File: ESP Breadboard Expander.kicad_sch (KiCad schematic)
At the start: 20 parts, among them J1 Conn_02x04_Odd_Even, J10 PJ-063BH, J2 Conn_01x08_Socket, J3 Conn_01x08_Socket, J4 Conn_01x19_Socket, J5 Conn_01x19_Socket, J6 Conn_01x14_Pin, J7 Conn_01x14_Pin, J8 Conn_01x02_Pin, J9 Conn_01x02_Pin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

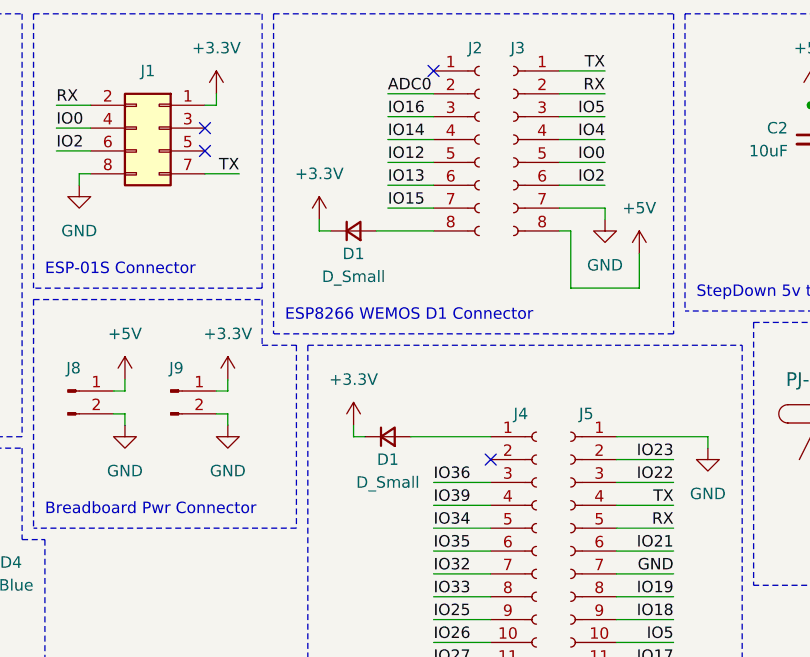
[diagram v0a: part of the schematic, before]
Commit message: Removed diode for 3.3V power from ESP to breadboard
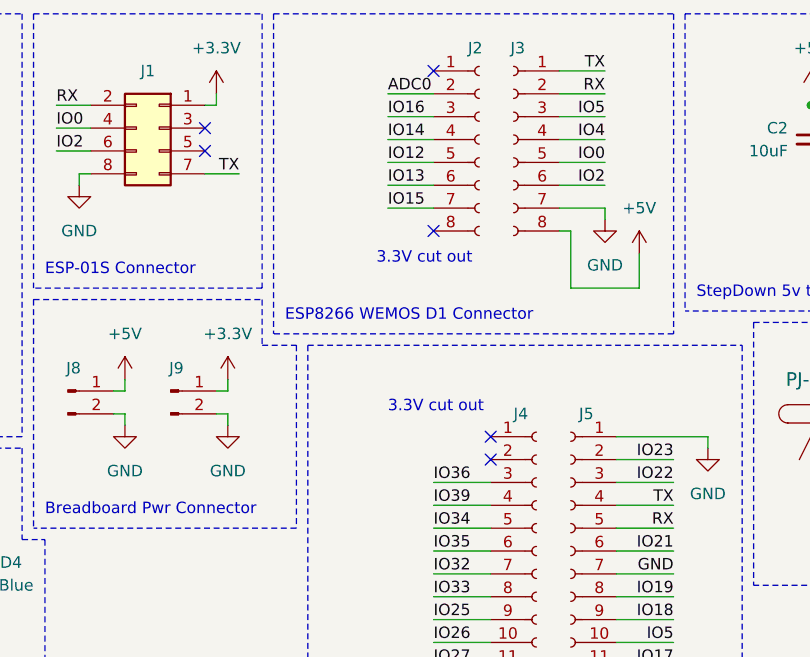
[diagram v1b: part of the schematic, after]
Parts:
- removed D1 (x2): D_Small, Diode_SMD:D_SMA, symbol Device:D_Small
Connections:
- no-connect marks 14 -> 16
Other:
- note added: "3.3V cut out"
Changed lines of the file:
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@@
   (junction (at 25.4 96.52) (diameter 0) (color 0 0 0 0)
   )
+  (no_connect (at 97.79 60.96))
   (no_connect (at 27.94 85.09))
   (no_connect (at 36.83 49.53))
+  (no_connect (at 91.44 38.1))
   (no_connect (at 91.44 20.32))
   (no_connect (at 97.79 99.06))
@@
     (stroke (width 0) (type dash))
   )
-  (wire (pts (xy 85.09 38.1) (xy 91.44 38.1))
-    (stroke (width 0) (type default))
-  )
   (wire (pts (xy 111.76 78.74) (xy 118.11 78.74))
     (stroke (width 0) (type default))
   )
-  (wire (pts (xy 78.74 36.83) (xy 78.74 38.1))
-    (stroke (width 0) (type default))
-  )
   (wire (pts (xy 16.51 34.29) (xy 22.86 34.29))
     (stroke (width 0) (type default))
@@
     (stroke (width 0) (type default))
   )
-  (wire (pts (xy 82.55 59.69) (xy 82.55 60.96))
-    (stroke (width 0) (type default))
-  )
-  (wire (pts (xy 78.74 38.1) (xy 80.01 38.1))
-    (stroke (width 0) (type default))
-  )
   (wire (pts (xy 30.48 96.52) (xy 27.94 96.52))
     (stroke (width 0) (type default))
@@
     (stroke (width 0) (type default))
   )
-  (wire (pts (xy 88.9 60.96) (xy 97.79 60.96))
-    (stroke (width 0) (type default))
-  )
   (wire (pts (xy 105.41 33.02) (xy 110.49 33.02))
     (stroke (width 0) (type default))
@@
   )
   (wire (pts (xy 105.41 27.94) (xy 110.49 27.94))
-    (stroke (width 0) (type default))
-  )
-  (wire (pts (xy 82.55 60.96) (xy 83.82 60.96))
     (stroke (width 0) (type default))
   )
@@
     (effects (font (size 1.27 1.27) (color 255 153 0 1)) (justify left bottom))
   )
+  (text "3.3V cut out" (at 86.36 58.42 0)
+    (effects (font (size 1.27 1.27) (color 255 0 255 1)) (justify left bottom))
+  )
   (text "ESP-01S Connector" (at 48.26 43.18 0)
     (effects (font (size 1.27 1.27) (color 255 153 0 1)) (justify left bottom))
@@
   (text "Breadboard Pwr Connector" (at 48.26 69.85 0)
     (effects (font (size 1.27 1.27) (color 255 153 0 1)) (justify left bottom))
+  )
+  (text "3.3V cut out" (at 85.09 41.91 0)
+    (effects (font (size 1.27 1.27) (color 255 0 255 1)) (justify left bottom))
   )
   (text "StepDown 5v to 3.3v\n" (at 120.65 45.72 0)
@@
     )
   )
-  (symbol (lib_id "power:+3.3V") (at 82.55 59.69 0) (unit 1)
-    (in_bom yes) (on_board yes) (dnp no) (fields_autoplaced)
-    (property "Reference" "#PWR013" (at 82.55 63.5 0)
-      (effects (font (size 1.27 1.27)) hide)
-    )
-    (property "Value" "+3.3V" (at 82.55 54.61 0)
-      (effects (font (size 1.27 1.27)))
-    )
-    (property "Footprint" "" (at 82.55 59.69 0)
-      (effects (font (size 1.27 1.27)) hide)
-    )
-    (property "Datasheet" "" (at 82.55 59.69 0)
-      (effects (font (size 1.27 1.27)) hide)
-    )
-    (pin "1")
-    (instances
-      (project "ESP Breadboard Expander"
-        (path "/cb783e29-3ea5-40c1-9e87-9edc5334a92e"
-          (reference "#PWR013") (unit 1)
-        )
-      )
-    )
-  )
   (symbol (lib_id "power:GND") (at 87.63 95.25 0) (unit 1)
     (in_bom yes) (on_board yes) (dnp no) (fields_autoplaced)
@@
         (path "/cb783e29-3ea5-40c1-9e87-9edc5334a92e"
           (reference "#PWR015") (unit 1)
-        )
-      )
-    )
-  )
-  (symbol (lib_id "Device:D_Small") (at 86.36 60.96 0) (unit 1)
-    (in_bom yes) (on_board yes) (dnp no)
-    (property "Reference" "D1" (at 86.36 63.5 0)
-      (effects (font (size 1.27 1.27)))
-    )
-    (property "Value" "D_Small" (at 86.36 66.04 0)
-      (effects (font (size 1.27 1.27)))
-    )
-    (property "Footprint" "Diode_SMD:D_SMA" (at 86.36 60.96 90)
-      (effects (font (size 1.27 1.27)) hide)
-    )
-    (property "Datasheet" "https://datasheet.lcsc.com/lcsc/2303141100_MDD-Microdiode-Electronics--SS34_C8678.pdf" (at 86.36 60.96 90)
-      (effects (font (size 1.27 1.27)) hide)
-    )
-    (property "Sim.Device" "D" (at 86.36 60.96 0)
-      (effects (font (size 1.27 1.27)) hide)
-    )
-    (property "Sim.Pins" "1=K 2=A" (at 86.36 60.96 0)
-      (effects (font (size 1.27 1.27)) hide)
-    )
-    (property "LCSC" "C8678" (at 86.36 60.96 0)
-      (effects (font (size 1.27 1.27)) hide)
-    )
-    (pin "1")
-    (pin "2")
-    (instances
-      (project "Doorbell"
-        (path "/1ebcbd1e-2253-497c-82d7-02fbe221a9cd"
-          (reference "D1") (unit 1)
-        )
-      )
-      (project "ESP Breadboard Expander"
-        (path "/cb783e29-3ea5-40c1-9e87-9edc5334a92e"
-          (reference "D4") (unit 1)
         )
       )
@@
         (path "/cb783e29-3ea5-40c1-9e87-9edc5334a92e"
           (reference "J8") (unit 1)
-        )
-      )
-    )
-  )
-  (symbol (lib_id "power:+3.3V") (at 78.74 36.83 0) (unit 1)
-    (in_bom yes) (on_board yes) (dnp no) (fields_autoplaced)
-    (property "Reference" "#PWR07" (at 78.74 40.64 0)
-      (effects (font (size 1.27 1.27)) hide)
-    )
-    (property "Value" "+3.3V" (at 78.74 31.75 0)
-      (effects (font (size 1.27 1.27)))
-    )
-    (property "Footprint" "" (at 78.74 36.83 0)
-      (effects (font (size 1.27 1.27)) hide)
-    )
-    (property "Datasheet" "" (at 78.74 36.83 0)
-      (effects (font (size 1.27 1.27)) hide)
-    )
-    (pin "1")
-    (instances
-      (project "ESP Breadboard Expander"
-        (path "/cb783e29-3ea5-40c1-9e87-9edc5334a92e"
-          (reference "#PWR07") (unit 1)
         )
       )
@@
         )
       )
-    )
-  )
-  (symbol (lib_id "Device:D_Small") (at 82.55 38.1 0) (unit 1)
-    (in_bom yes) (on_board yes) (dnp no)
-    (property "Reference" "D1" (at 82.55 40.64 0)
-      (effects (font (size 1.27 1.27)))
-    )
-    (property "Value" "D_Small" (at 82.55 43.18 0)
-      (effects (font (size 1.27 1.27)))
-    )
-    (property "Footprint" "Diode_SMD:D_SMA" (at 82.55 38.1 90)
-      (effects (font (size 1.27 1.27)) hide)
-    )
-    (property "Datasheet" "https://datasheet.lcsc.com/lcsc/2303141100_MDD-Microdiode-Electronics--SS34_C8678.pdf" (at 82.55 38.1 90)
-      (effects (font (size 1.27 1.27)) hide)
-    )
-    (property "Sim.Device" "D" (at 82.55 38.1 0)
-      (effects (font (size 1.27 1.27)) hide)
-    )
-    (property "Sim.Pins" "1=K 2=A" (at 82.55 38.1 0)
-      (effects (font (size 1.27 1.27)) hide)
-    )
-    (property "LCSC" "C8678" (at 82.55 38.1 0)
-      (effects (font (size 1.27 1.27)) hide)
-    )
-    (pin "1")
-    (pin "2")
-    (instances
-      (project "Doorbell"
-        (path "/1ebcbd1e-2253-497c-82d7-02fbe221a9cd"
-          (reference "D1") (unit 1)
-        )
-      )
-      (project "ESP Breadboard Expander"
-        (path "/cb783e29-3ea5-40c1-9e87-9edc5334a92e"
-          (reference "D5") (unit 1)
-        )
-      )

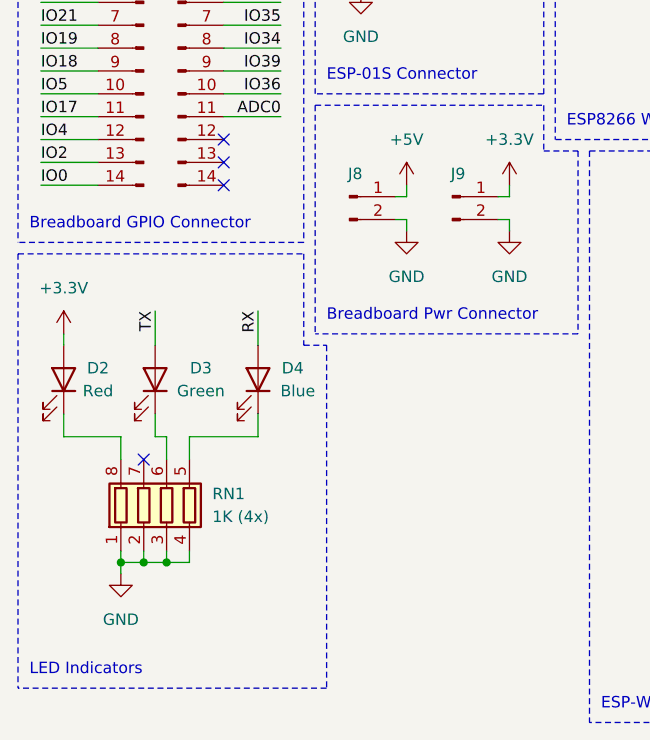
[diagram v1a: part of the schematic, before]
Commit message: Fixed a number of issues to work with JLCPCB
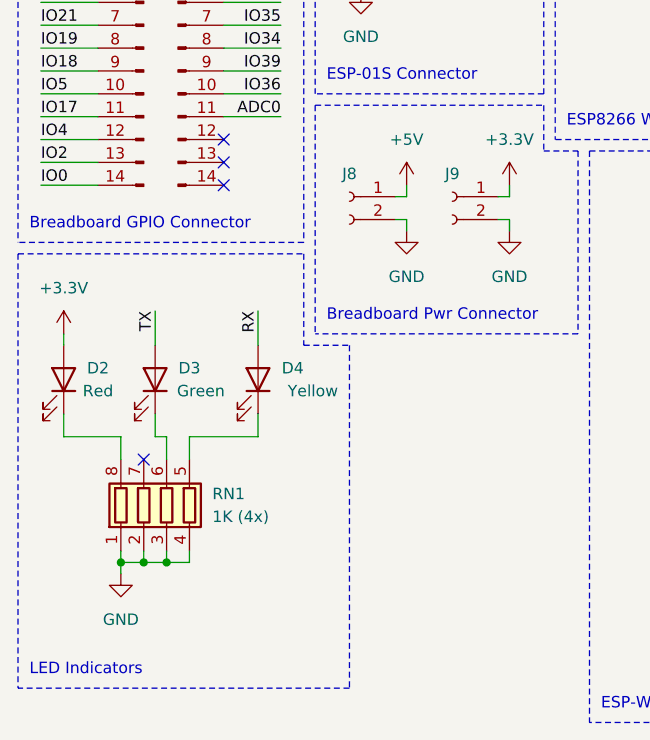
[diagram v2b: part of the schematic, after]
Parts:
- removed J8, J9: Conn_01x02_Pin, Adam_Custom_Footprints:PinHeader_1x02_P2.54mm_Vertical_UpSideDown, symbol Connector:Conn_01x02_Pin
- added J8, J9: Conn_01x02_Socket, Connector_PinSocket_2.54mm:PinSocket_1x02_P2.54mm_Vertical, symbol Connector:Conn_01x02_Socket
- D4: value Blue -> Yellow; LCSC C72041 -> C72038
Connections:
- net +3.3V: now also J9.1 (Pin_1)
- net +5V: now also J8.1 (Pin_1)
- net GND: now also J8.2 (Pin_2), J9.2 (Pin_2)
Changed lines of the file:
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@@
     (stroke (width 0) (type dash))
   )
-  (polyline (pts (xy 48.26 72.39) (xy 48.26 110.49))
+  (polyline (pts (xy 50.8 72.39) (xy 50.8 110.49))
     (stroke (width 0) (type dash))
   )
@@
     (stroke (width 0) (type default))
   )
-  (polyline (pts (xy 45.72 72.39) (xy 48.26 72.39))
+  (polyline (pts (xy 45.72 72.39) (xy 50.8 72.39))
     (stroke (width 0) (type dash))
   )
@@
     (stroke (width 0) (type default))
   )
-  (polyline (pts (xy 48.26 110.49) (xy 13.97 110.49))
+  (polyline (pts (xy 50.8 110.49) (xy 13.97 110.49))
     (stroke (width 0) (type dash))
   )
@@
     )
   )
+  (symbol (lib_id "Connector:Conn_01x02_Socket") (at 62.23 55.88 0) (mirror y) (unit 1)
+    (in_bom yes) (on_board yes) (dnp no)
+    (property "Reference" "J9" (at 62.23 53.34 0)
+      (effects (font (size 1.27 1.27)))
+    )
+    (property "Value" "Conn_01x02_Socket" (at 62.865 53.34 0)
+      (effects (font (size 1.27 1.27)) hide)
+    )
+    (property "Footprint" "Connector_PinSocket_2.54mm:PinSocket_1x02_P2.54mm_Vertical" (at 62.23 55.88 0)
+      (effects (font (size 1.27 1.27)) hide)
+    )
+    (property "Datasheet" "~" (at 62.23 55.88 0)
+      (effects (font (size 1.27 1.27)) hide)
+    )
+    (property "LCSC" "" (at 62.23 55.88 0)
+      (effects (font (size 1.27 1.27)) hide)
+    )
+    (pin "2")
+    (pin "1")
+    (instances
+      (project "ESP Breadboard Expander"
+        (path "/cb783e29-3ea5-40c1-9e87-9edc5334a92e"
+          (reference "J9") (unit 1)
+        )
+      )
+    )
+  )
   (symbol (lib_id "Device:LED") (at 19.05 76.2 270) (mirror x) (unit 1)
     (in_bom yes) (on_board yes) (dnp no)
@@
   (symbol (lib_id "Device:LED") (at 29.21 76.2 270) (mirror x) (unit 1)
     (in_bom yes) (on_board yes) (dnp no)
-    (property "Reference" "D3" (at 34.29 74.93 90)
+    (property "Reference" "D3" (at 33.02 74.93 90)
       (effects (font (size 1.27 1.27)))
     )
@@
       (effects (font (size 1.27 1.27)) (justify right))
     )
-    (property "Value" "Blue" (at 46.99 77.47 90)
-      (effects (font (size 1.27 1.27) (color 0 255 255 1)) (justify right))
+    (property "Value" "Yellow" (at 49.53 77.47 90)
+      (effects (font (size 1.27 1.27) (color 255 255 0 1)) (justify right))
     )
     (property "Footprint" "LED_SMD:LED_0603_1608Metric" (at 40.64 76.2 0)
@@
       (effects (font (size 1.27 1.27)) hide)
     )
-    (property "LCSC" "C72041" (at 40.64 76.2 0)
+    (property "LCSC" "C72038" (at 40.64 76.2 0)
       (effects (font (size 1.27 1.27)) hide)
     )
@@
         (path "/cb783e29-3ea5-40c1-9e87-9edc5334a92e"
           (reference "#PWR04") (unit 1)
-        )
-      )
-    )
-  )
-  (symbol (lib_id "Connector:Conn_01x02_Pin") (at 50.8 55.88 0) (unit 1)
-    (in_bom yes) (on_board yes) (dnp no) (fields_autoplaced)
-    (property "Reference" "J8" (at 51.435 53.34 0)
-      (effects (font (size 1.27 1.27)))
-    )
-    (property "Value" "Conn_01x02_Pin" (at 51.435 53.34 0)
-      (effects (font (size 1.27 1.27)) hide)
-    )
-    (property "Footprint" "Adam_Custom_Footprints:PinHeader_1x02_P2.54mm_Vertical_UpSideDown" (at 50.8 55.88 0)
-      (effects (font (size 1.27 1.27)) hide)
-    )
-    (property "Datasheet" "~" (at 50.8 55.88 0)
-      (effects (font (size 1.27 1.27)) hide)
-    )
-    (property "LCSC" "" (at 50.8 55.88 0)
-      (effects (font (size 1.27 1.27)) hide)
-    )
-    (pin "1")
-    (pin "2")
-    (instances
-      (project "ESP Breadboard Expander"
-        (path "/cb783e29-3ea5-40c1-9e87-9edc5334a92e"
-          (reference "J8") (unit 1)
         )
       )
@@
     )
   )
-  (symbol (lib_id "Connector:Conn_01x02_Pin") (at 62.23 55.88 0) (unit 1)
-    (in_bom yes) (on_board yes) (dnp no) (fields_autoplaced)
-    (property "Reference" "J9" (at 62.865 53.34 0)
-      (effects (font (size 1.27 1.27)))
-    )
-    (property "Value" "Conn_01x02_Pin" (at 62.865 53.34 0)
-      (effects (font (size 1.27 1.27)) hide)
-    )
-    (property "Footprint" "Adam_Custom_Footprints:PinHeader_1x02_P2.54mm_Vertical_UpSideDown" (at 62.23 55.88 0)
-      (effects (font (size 1.27 1.27)) hide)
-    )
-    (property "Datasheet" "~" (at 62.23 55.88 0)
-      (effects (font (size 1.27 1.27)) hide)
-    )
-    (property "LCSC" "" (at 62.23 55.88 0)
-      (effects (font (size 1.27 1.27)) hide)
-    )
-    (pin "1")
-    (pin "2")
-    (instances
-      (project "ESP Breadboard Expander"
-        (path "/cb783e29-3ea5-40c1-9e87-9edc5334a92e"
-          (reference "J9") (unit 1)
-        )
-      )
-    )
-  )
   (symbol (lib_id "power:+5V") (at 167.64 57.15 0) (unit 1)
     (in_bom yes) (on_board yes) (dnp no) (fields_autoplaced)
@@
         )
       )
+    )
+  )
+  (symbol (lib_id "Connector:Conn_01x02_Socket") (at 50.8 55.88 0) (mirror y) (unit 1)
+    (in_bom yes) (on_board yes) (dnp no)
+    (property "Reference" "J8" (at 50.8 53.34 0)
+      (effects (font (size 1.27 1.27)))
+    )
+    (property "Value" "Conn_01x02_Socket" (at 51.435 53.34 0)
+      (effects (font (size 1.27 1.27)) hide)
+    )
+    (property "Footprint" "Connector_PinSocket_2.54mm:PinSocket_1x02_P2.54mm_Vertical" (at 50.8 55.88 0)
+      (effects (font (size 1.27 1.27)) hide)
+    )
+    (property "Datasheet" "~" (at 50.8 55.88 0)
+      (effects (font (size 1.27 1.27)) hide)
+    )
+    (property "LCSC" "" (at 50.8 55.88 0)
+      (effects (font (size 1.27 1.27)) hide)
+    )
+    (pin "2")
+    (pin "1")
+    (instances
+      (project "ESP Breadboard Expander"
+        (path "/cb783e29-3ea5-40c1-9e87-9edc5334a92e"
+          (reference "J8") (unit 1)
+        )
+      )
